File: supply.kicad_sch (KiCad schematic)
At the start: 139 parts, among them J10002 PinHeader_1x3_P2.54mm_Drill1.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, J1001 BarrelJack_3167288, Q10001 BSS138PW, Q1001 SI7613DN-T1-GE3, Q1002 BSS138PW, SW1001 SW_CVS-02B, SW1002 SW_KMR211NGLFS_SMD, U10001 NCP718BSN330T1G, U10002 MPM54304GMN, U10003 MPM54304GMN, U10004 MAX16150A_SOT, U10006 LM3880, U10007 MP8869S, U10008 XC6230H001ER-G, U10009 MAX812REUS+T, U1001 LTC4412IS6, U10010 PAC1954T-E_VQFN, U10011 PAC1954T-E_VQFN

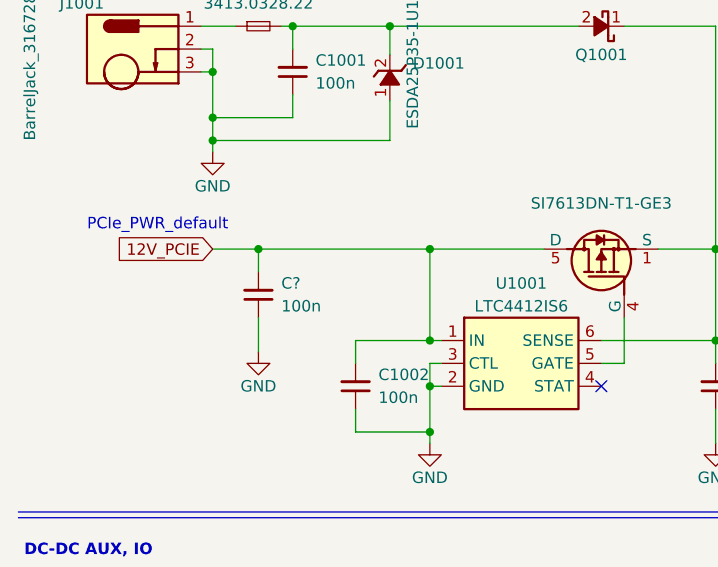
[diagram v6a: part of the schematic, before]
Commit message: Create FPGA decoupling, start creating power planes
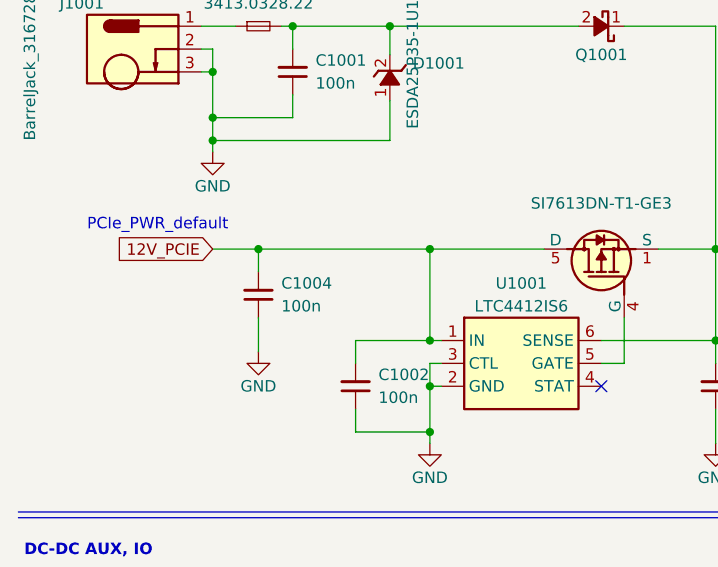
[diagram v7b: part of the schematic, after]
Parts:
- gave numbers to parts that had none: 1
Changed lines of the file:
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@@
   (symbol (lib_id "DM3390_Connector_A-altium-import:GND") (at 38.735 59.69 0) (unit 1)
     (in_bom yes) (on_board yes) (fields_autoplaced)
-    (property "Reference" "#PWR?" (id 0) (at 38.735 66.04 0)
+    (property "Reference" "#PWR0178" (id 0) (at 38.735 66.04 0)
       (effects (font (size 1.27 1.27)) hide)
     )
@@
   (symbol (lib_id "antmicroCapacitors0402:C_100n_0402") (at 38.735 55.88 90) (unit 1)
     (in_bom yes) (on_board yes) (fields_autoplaced)
-    (property "Reference" "C?" (id 0) (at 41.275 52.0635 90)
-      (effects (font (size 1.27 1.27)) (justify right))
-    )
+    (property "Reference" "C1004" (id 0) (at 41.275 52.0635 90)
+      (effects (font (size 1.27 1.27)) (justify right))
+    )

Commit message: Schematic cleanup, connect VINT DC-DC, continue placing misc. circuits
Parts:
- removed D1002: PMEG3050EP,115, antmicro-footprints:Nexperia_SOD128, symbol antmicroDiodesRectifiersSingle:PMEG3050EP,115
- removed J10002: PinHeader_1x3_P2.54mm_Drill1.1mm, data-center-rdimm-ddr4-tester-footprints:PinHeader_1x3_P2.54_Drill1.1mm, symbol data-center-rdimm-ddr4-tester:PinHeader_1x3_P2.54mm_Drill1.1mm
- added C10022: C_100n_0402, antmicro-footprints:C_0402_1005Metric, symbol antmicroCapacitors0402:C_100n_0402
- added C10038: C_1u_25V_0603, antmicro-footprints:C_0603_1608Metric, symbol antmicroCapacitors0603:C_1u_25V_0603
- added C10042: C_1u_0402, antmicro-footprints:C_0402_1005Metric, symbol antmicroCapacitors0402:C_1u_0402
- added J10001: JST_SH_1x4_BM04B-SRSS-TB-LF-SN, antmicro-footprints:Conn_JST_SH_1x4_BM04B-SRSS-TB-LF-SN, symbol antmicroWire2BoardConnectors:JST_SH_1x4_BM04B-SRSS-TB-LF-SN
- added Q10002: SI7613DN-T1-GE3, antmicro-footprints:Vishay_PowerPAK_1212-8_Single, symbol antmicroTransistorsFETsMOSFETsSingle:SI7613DN-T1-GE3
- added U10005: LTC4412IS6, antmicro-footprints:SOT-23-6, symbol antmicroPMICORControllersIdealDiodes:LTC4412IS6
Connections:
- net +5V: now also C10042.2, J10001.2 (Pin_2)
- net GND: now also C10022.1, C10038.1, C10042.1, J10001.1 (Pin_1), J10001.MP, U10005.2 (GND), U10005.3 (CTL)
- net VDC: now also C10038.2, Q10002.1 (S), Q10002.2 (S), Q10002.3 (S), U10005.6 (SENSE)
- net at C1001.2, D1001.2 (A): now also F1001.1, J1001.1; no longer F1001.2
- new net: C10022.2, F1001.2, Q10002.5 (D), U10005.1 (IN)
- new net: Q10002.4 (G), U10005.5 (GATE)
- no-connect marks 7 -> 8
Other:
- moved on the sheet: C10002, C10003, C10004, C10005, C10007, C10008, C10009, C1001, C10010, C10011, C10012, C10013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
